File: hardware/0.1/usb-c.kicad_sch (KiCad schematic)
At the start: 30 parts, among them J201 USB_C_Receptacle, U201 TPD4EUSB30, U202 HD3SS3220, U203 TPD4EUSB30, U204 TPD4EUSB30

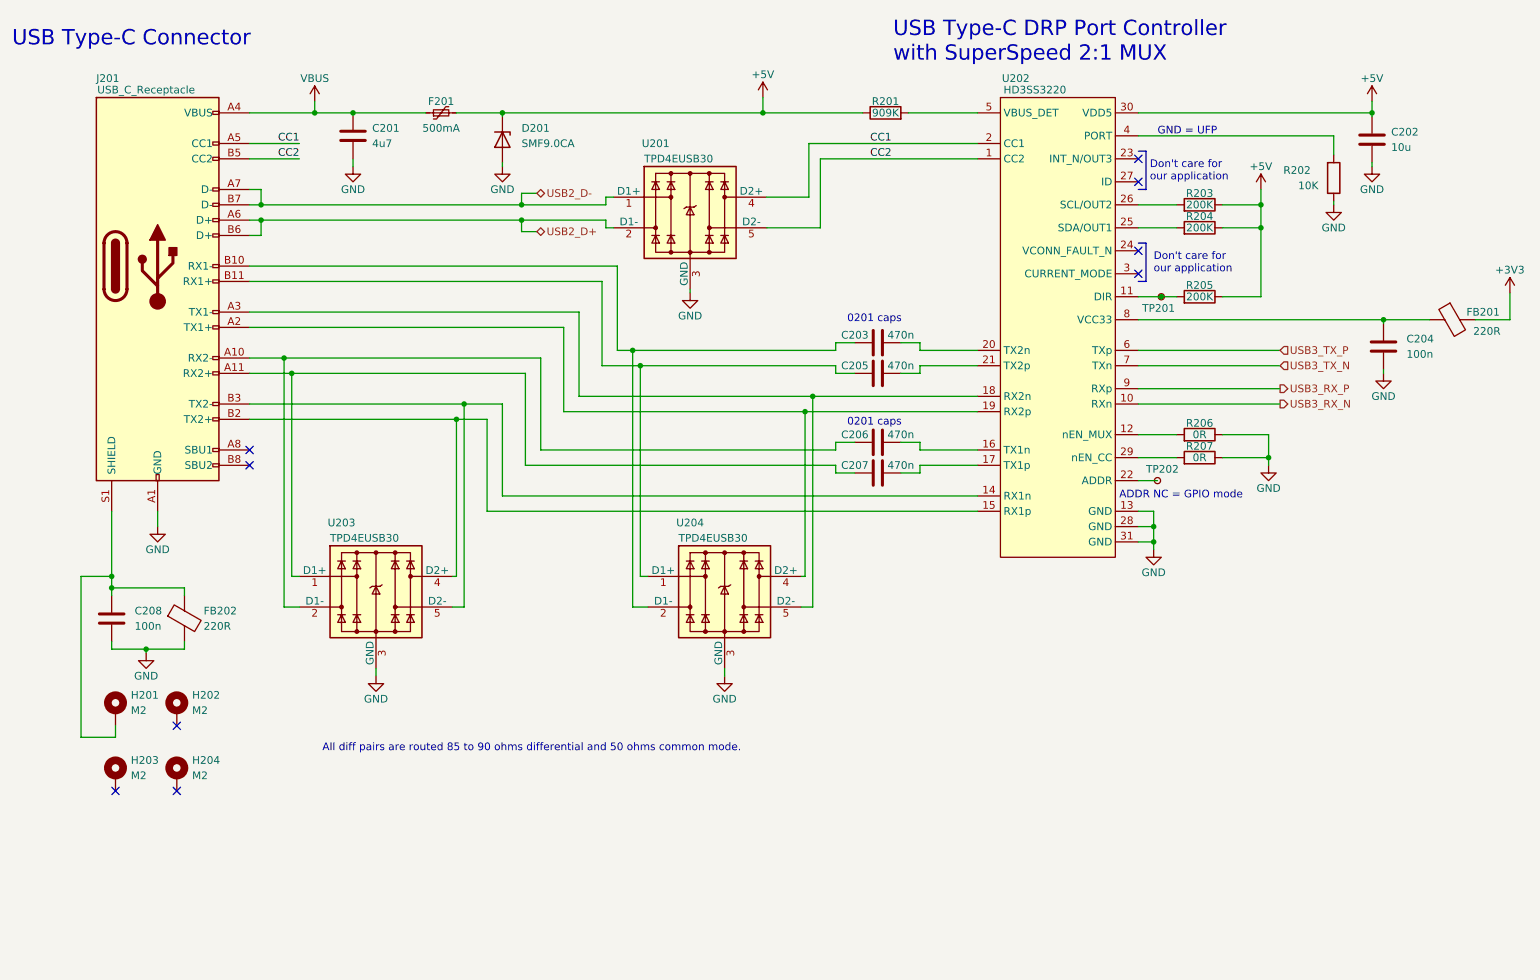
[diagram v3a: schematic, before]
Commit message: break out bga
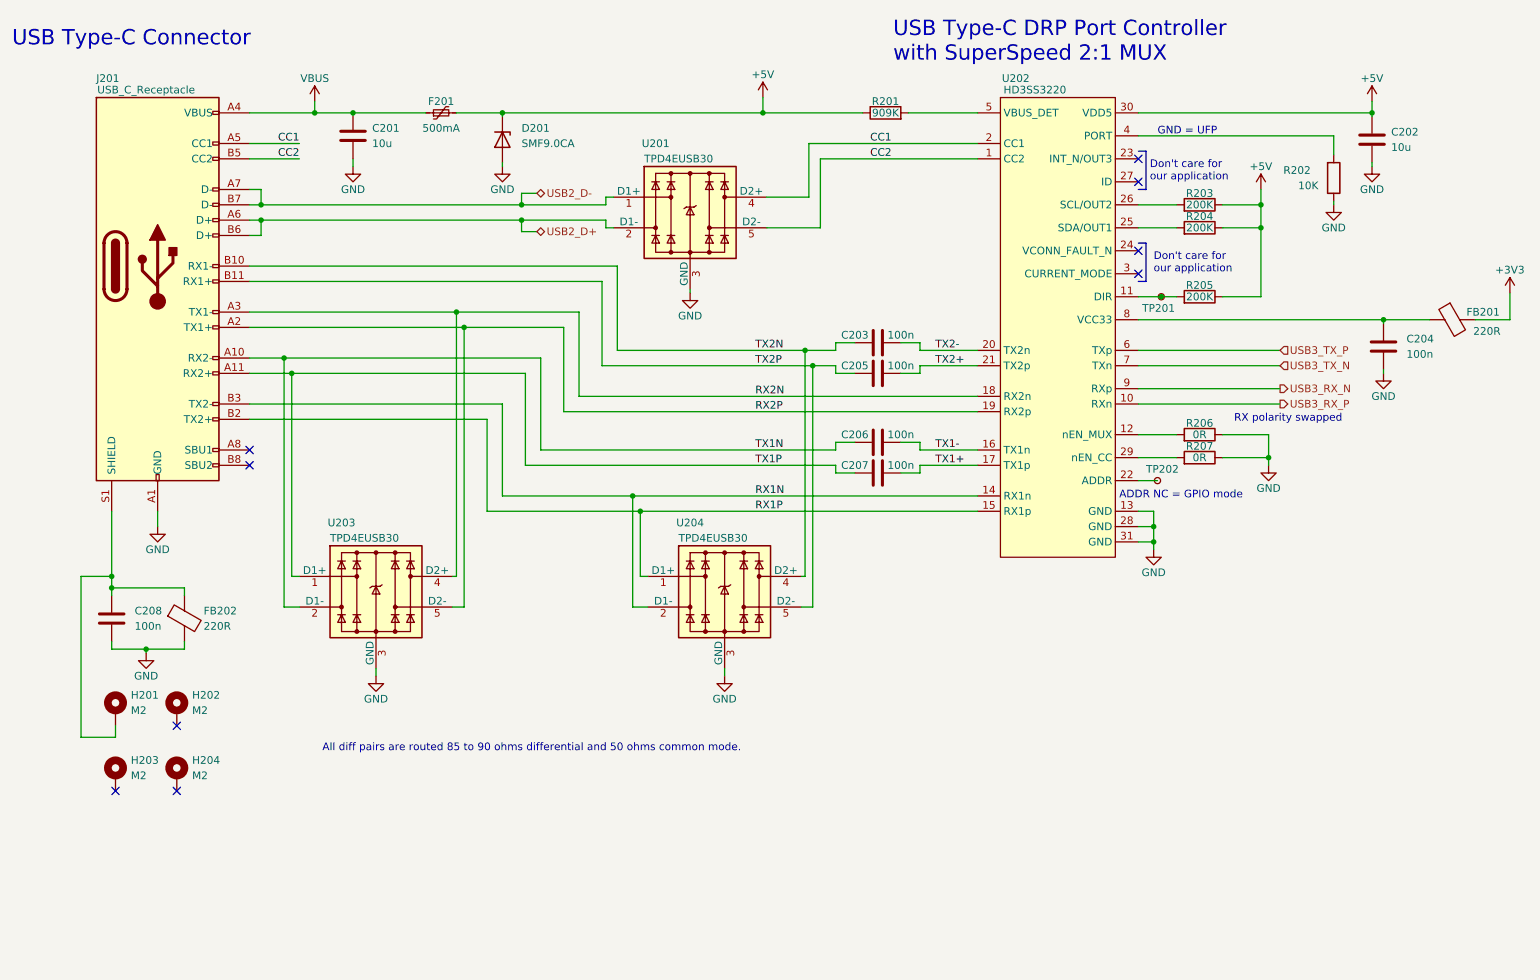
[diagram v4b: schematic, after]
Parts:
- C201: value 4u7 -> 10u; footprint Capacitor_SMD:C_0402_1005Metric -> Capacitor_SMD:C_0603_1608Metric; LCSC C23733 -> (none); MPN CL05A475MP5NRNC -> (none); Manufacturer Samsung Electro-Mechanics -> (none)
- C203, C205, C206, C207: value 470n -> 100n; footprint Capacitor_SMD:C_0402_1005Metric -> Capacitor_SMD:C_0201_0603Metric
- F201: footprint josh-passives-smt:Fuse_0603_1608Metric -> josh-passives-smt:Fuse_0805_2012Metric; LCSC C210357 -> (none); MPN MF-FSMF050X-2 -> (none); Manufacturer Bourns -> (none)
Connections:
- net USB3_RX_N: now also U202.9 (RXp); no longer U202.10 (RXn)
- net USB3_RX_P: now also U202.10 (RXn); no longer U202.9 (RXp)
- net TX1P: now reaches C207.1, J201.A11 (RX2+), U203.1 (D1+)
- net TX1N: now reaches C206.1, J201.A10 (RX2-), U203.2 (D1-)
- net RX1P: now reaches J201.B2 (TX2+), U202.15 (RX1p)
- net RX1P: now also U204.1 (D1+); no longer U203.4 (D2+)
- net RX1N: now reaches J201.B3 (TX2-), U202.14 (RX1n)
- net RX1N: now also U204.2 (D1-); no longer U203.5 (D2-)
- net TX2P: now reaches C205.1, J201.B11 (RX1+)
- net TX2P: now also U204.5 (D2-); no longer U204.1 (D1+)
- net TX2+: now reaches C205.2, U202.21 (TX2p)
- net TX2N: now reaches C203.1, J201.B10 (RX1-)
- net TX2N: now also U204.4 (D2+); no longer U204.2 (D1-)
- net RX2P: now reaches J201.A2 (TX1+), U202.19 (RX2p)
- net RX2P: now also U203.5 (D2-); no longer U204.4 (D2+)
- net RX2N: now reaches J201.A3 (TX1-), U202.18 (RX2n)
- net RX2N: now also U203.4 (D2+); no longer U204.5 (D2-)
- net TX1+: now reaches C207.2, U202.17 (TX1p)
- net TX1-: now reaches C206.2, U202.16 (TX1n)
- net TX2-: now reaches C203.2, U202.20 (TX2n)
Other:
- note added: "RX polarity swapped"
- note removed: "0201 caps"

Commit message: usb3 routed less tuning
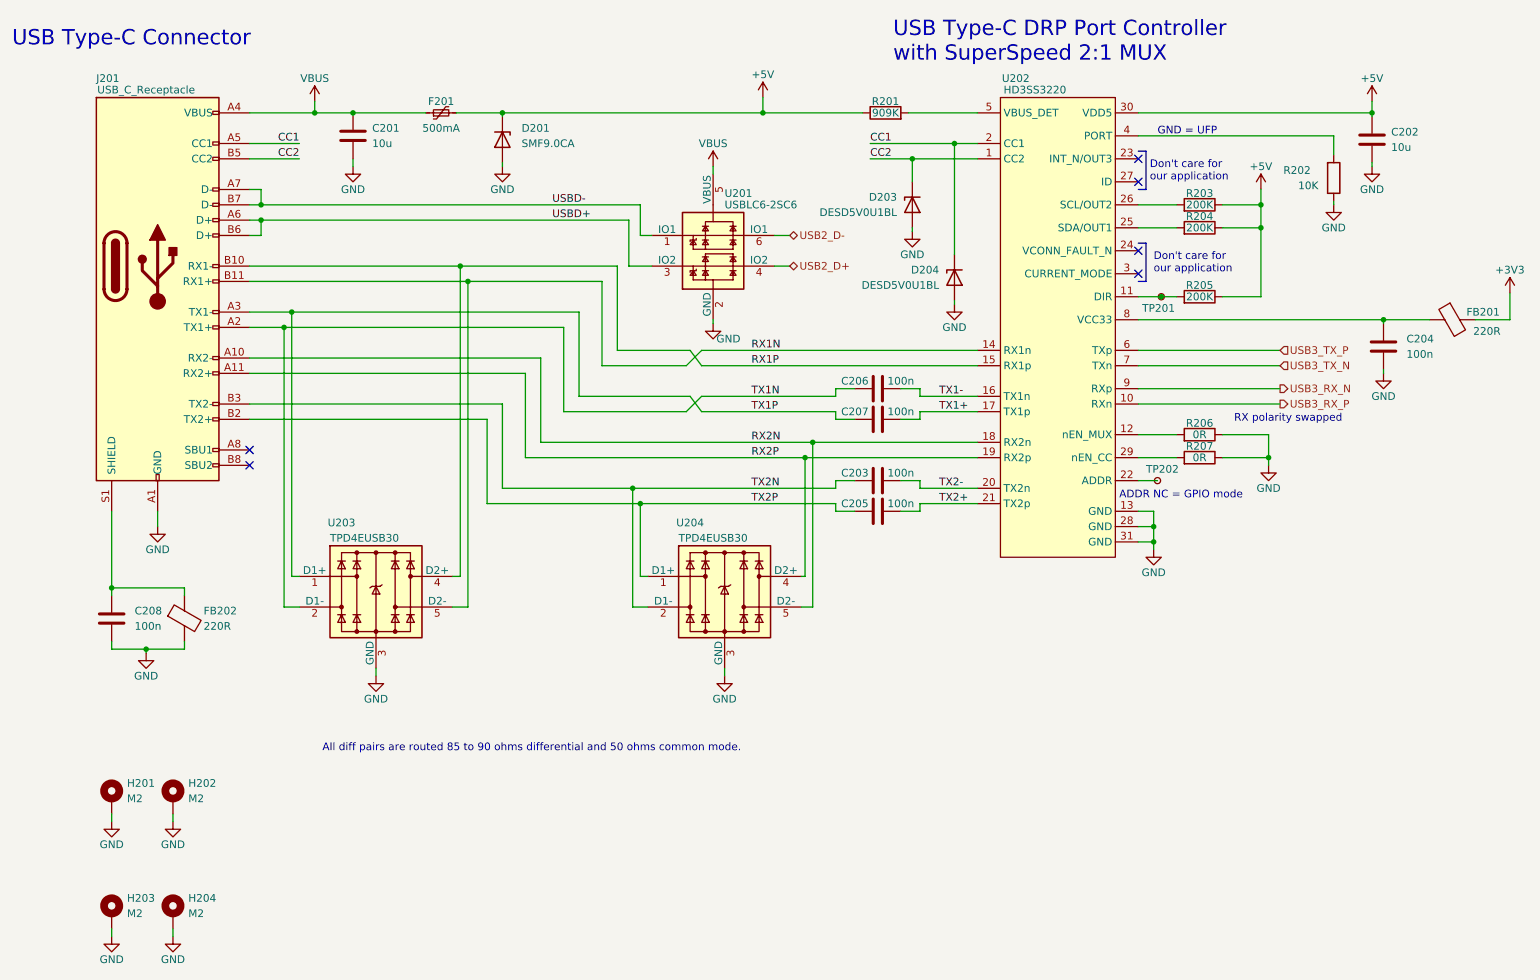
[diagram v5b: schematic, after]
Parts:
- removed U201: TPD4EUSB30, Package_SON:USON-10_2.5x1.0mm_P0.5mm, symbol Power_Protection:TPD4EUSB30
- added D203, D204: DESD5V0U1BL, josh-passives-smt:D_X1-DFN1006-2, symbol Device:D_Zener
- added U201: USBLC6-2SC6, josh-soic-sot-etc:SOT-563, symbol josh-ic:USBLC6-2SC6
- U203, U204: symbol Power_Protection:TPD4EUSB30 -> josh-ic:TPD4EUSB30
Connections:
- net CC1: now also D204.1 (K)
- net CC2: now also D203.1 (K)
- net GND: now also H201.1, H202.1, H203.1, H204.1, D203.2 (A), D204.2 (A), U201.2 (GND)
- net RX1N: now also J201.B11 (RX1+), U203.5 (D2-), U203.6 (NC); no longer J201.B3 (TX2-), U204.2 (D1-)
- net RX1P: now also J201.B10 (RX1-), U203.4 (D2+), U203.7 (NC); no longer J201.B2 (TX2+), U204.1 (D1+)
- net RX2N: now also J201.A10 (RX2-), U204.5 (D2-), U204.6 (NC); no longer J201.A3 (TX1-), U203.4 (D2+)
- net RX2P: now also J201.A11 (RX2+), U204.4 (D2+), U204.7 (NC); no longer J201.A2 (TX1+), U203.5 (D2-)
- net TX1N: now also J201.A2 (TX1+), U203.9 (NC); no longer J201.A10 (RX2-)
- net TX1P: now also J201.A3 (TX1-), U203.10 (NC); no longer J201.A11 (RX2+)
- net TX2N: now also J201.B3 (TX2-), U204.2 (D1-), U204.9 (NC); no longer J201.B10 (RX1-), U204.4 (D2+)
- net TX2P: now also J201.B2 (TX2+), U204.1 (D1+), U204.10 (NC); no longer J201.B11 (RX1+), U204.5 (D2-)
- net USB2_D+: now also U201.4 (IO2); no longer J201.A6 (D+), J201.B6 (D+)
- net USB2_D-: now also U201.6 (IO1); no longer J201.A7 (D-), J201.B7 (D-)
- net VBUS: now also U201.5 (VBUS)
- net at C208.1, FB202.1, J201.S1 (SHIELD): no longer H201.1
- new net USBD+: J201.A6 (D+), J201.B6 (D+), U201.3 (IO2)
- new net USBD-: J201.A7 (D-), J201.B7 (D-), U201.1 (IO1)
- no-connect marks 9 -> 6
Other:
- moved on the sheet: C203, C205, C206, C207, H201, H202, H203, H204

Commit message: wip, switchers todo
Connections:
- net SHIELD: now reaches C208.1, FB202.1, J201.S1 (SHIELD)
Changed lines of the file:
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@@
+    (effects (font (size 1.27 1.27)) (justify left bottom))
+  )
+  (label "SHIELD" (at 41.91 133.985 0)
     (effects (font (size 1.27 1.27)) (justify left bottom))
   )

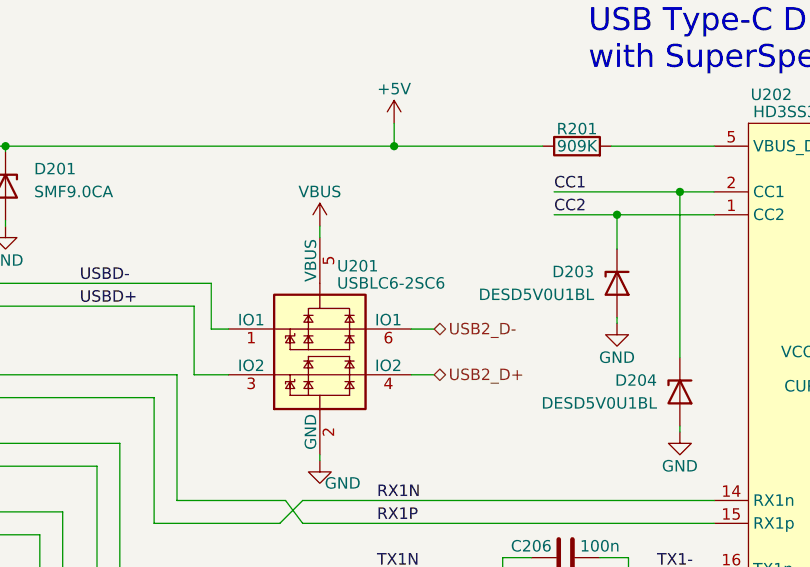
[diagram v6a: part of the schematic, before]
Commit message: erc = drc = 0, fixup BOM
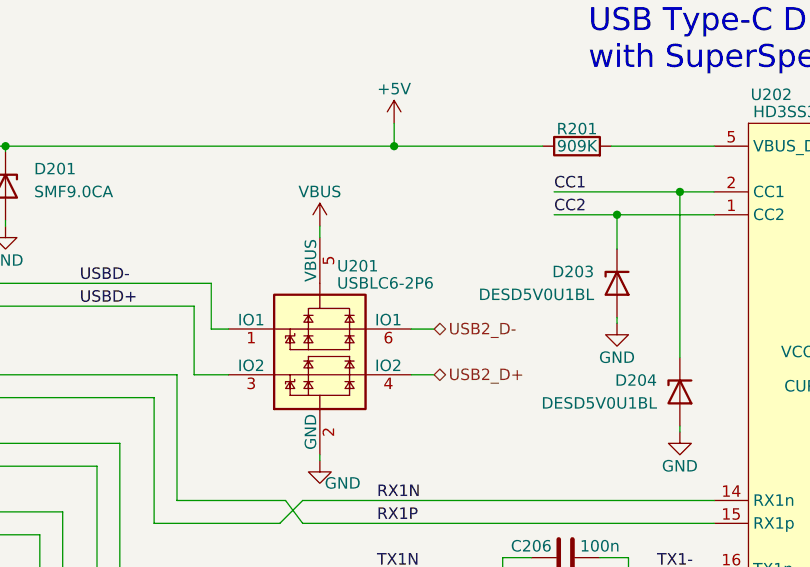
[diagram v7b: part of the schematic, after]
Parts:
- C201: LCSC (none) -> C96446; MPN (none) -> CL10A106MA8NRNC; Manufacturer (none) -> Samsung Electro-Mechanics
- C203, C205, C206, C207: LCSC (none) -> C307380; MPN (none) -> CL03A104KO3NNNC; Manufacturer (none) -> Samsung Electro-Mechanics
- F201: LCSC (none) -> C66452; MPN (none) -> SMD0805-050; Manufacturer (none) -> TECHFUSE
- H201, H202, H203, H204: now left out of the parts list
- R206, R207: MPN RC0402FR-070RL -> C106231; Manufacturer Yageo -> C106231
- U201: value USBLC6-2SC6 -> USBLC6-2P6; LCSC (none) -> C15999; MPN (none) -> USBLC6-2P6; Manufacturer (none) -> STMicroelectronics
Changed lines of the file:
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@@
       (effects (font (size 1.27 1.27)) hide)
     )
-    (property "LCSC" "" (id 4) (at 78.105 59.055 0)
-      (effects (font (size 1.27 1.27)) hide)
-    )
-    (property "MPN" "" (id 5) (at 78.105 59.055 0)
-      (effects (font (size 1.27 1.27)) hide)
-    )
-    (property "Manufacturer" "" (id 6) (at 78.105 59.055 0)
+    (property "LCSC" "C96446" (id 4) (at 78.105 59.055 0)
+      (effects (font (size 1.27 1.27)) hide)
+    )
+    (property "MPN" "CL10A106MA8NRNC" (id 5) (at 78.105 59.055 0)
+      (effects (font (size 1.27 1.27)) hide)
+    )
+    (property "Manufacturer" "Samsung Electro-Mechanics" (id 6) (at 78.105 59.055 0)
       (effects (font (size 1.27 1.27)) hide)
     )
@@
   )
   (symbol (lib_id "Mechanical:MountingHole_Pad") (at 38.1 168.91 0) (unit 1)
-    (in_bom yes) (on_board yes) (fields_autoplaced)
+    (in_bom no) (on_board yes) (fields_autoplaced)
     (property "Reference" "H201" (id 0) (at 40.64 166.3699 0)
       (effects (font (size 1.27 1.27)) (justify left))
@@
     )
     (property "Datasheet" "~" (id 3) (at 165.1 121.285 0)
+      (effects (font (size 1.27 1.27)) hide)
+    )
+    (property "LCSC" "C307380" (id 4) (at 165.1 121.285 0)
+      (effects (font (size 1.27 1.27)) hide)
+    )
+    (property "MPN" "CL03A104KO3NNNC" (id 5) (at 165.1 121.285 0)
+      (effects (font (size 1.27 1.27)) hide)
+    )
+    (property "Manufacturer" "Samsung Electro-Mechanics" (id 6) (at 165.1 121.285 0)
       (effects (font (size 1.27 1.27)) hide)
     )
@@
   )
   (symbol (lib_id "Mechanical:MountingHole_Pad") (at 48.26 168.91 0) (unit 1)
-    (in_bom yes) (on_board yes) (fields_autoplaced)
+    (in_bom no) (on_board yes) (fields_autoplaced)
     (property "Reference" "H202" (id 0) (at 50.8 166.3699 0)
       (effects (font (size 1.27 1.27)) (justify left))
@@
       (effects (font (size 1.27 1.27)) hide)
     )
-    (property "MPN" "RC0402FR-070RL" (id 5) (at 218.44 108.585 0)
-      (effects (font (size 1.27 1.27)) hide)
-    )
-    (property "Manufacturer" "Yageo" (id 6) (at 218.44 108.585 0)
+    (property "MPN" "C106231" (id 5) (at 218.44 108.585 0)
+      (effects (font (size 1.27 1.27)) hide)
+    )
+    (property "Manufacturer" "C106231" (id 6) (at 218.44 108.585 0)
       (effects (font (size 1.27 1.27)) hide)
     )
@@
     )
     (property "Datasheet" "~" (id 3) (at 165.1 106.045 0)
+      (effects (font (size 1.27 1.27)) hide)
+    )
+    (property "LCSC" "C307380" (id 4) (at 165.1 106.045 0)
+      (effects (font (size 1.27 1.27)) hide)
+    )
+    (property "MPN" "CL03A104KO3NNNC" (id 5) (at 165.1 106.045 0)
+      (effects (font (size 1.27 1.27)) hide)
+    )
+    (property "Manufacturer" "Samsung Electro-Mechanics" (id 6) (at 165.1 106.045 0)
       (effects (font (size 1.27 1.27)) hide)
     )
@@
       (effects (font (size 1.27 1.27)) hide)
     )
-    (property "MPN" "RC0402FR-070RL" (id 5) (at 218.44 112.395 0)
-      (effects (font (size 1.27 1.27)) hide)
-    )
-    (property "Manufacturer" "Yageo" (id 6) (at 218.44 112.395 0)
+    (property "MPN" "C106231" (id 5) (at 218.44 112.395 0)
+      (effects (font (size 1.27 1.27)) hide)
+    )
+    (property "Manufacturer" "C106231" (id 6) (at 218.44 112.395 0)
       (effects (font (size 1.27 1.27)) hide)
     )
@@
   )
   (symbol (lib_id "Mechanical:MountingHole_Pad") (at 48.26 187.96 0) (unit 1)
-    (in_bom yes) (on_board yes) (fields_autoplaced)
+    (in_bom no) (on_board yes) (fields_autoplaced)
     (property "Reference" "H204" (id 0) (at 50.8 185.4199 0)
       (effects (font (size 1.27 1.27)) (justify left))
@@
       (effects (font (size 1.27 1.27)) (justify left))
     )
-    (property "Value" "USBLC6-2SC6" (id 1) (at 139.7 70.485 0)
+    (property "Value" "USBLC6-2P6" (id 1) (at 139.7 70.485 0)
       (effects (font (size 1.27 1.27)) (justify left))
     )
@@
     )
     (property "Datasheet" "http://www2.st.com/resource/en/datasheet/CD00050750.pdf" (id 3) (at 142.875 69.215 0)
+      (effects (font (size 1.27 1.27)) hide)
+    )
+    (property "LCSC" "C15999" (id 4) (at 137.795 78.105 0)
+      (effects (font (size 1.27 1.27)) hide)
+    )
+    (property "MPN" "USBLC6-2P6" (id 5) (at 137.795 78.105 0)
+      (effects (font (size 1.27 1.27)) hide)
+    )
+    (property "Manufacturer" "STMicroelectronics" (id 6) (at 137.795 78.105 0)
       (effects (font (size 1.27 1.27)) hide)
     )
@@
       (effects (font (size 1.27 1.27)) hide)
     )
-    (property "MPN" "" (id 4) (at 92.71 55.245 0)
-      (effects (font (size 1.27 1.27)) hide)
-    )
-    (property "Manufacturer" "" (id 5) (at 92.71 55.245 0)
-      (effects (font (size 1.27 1.27)) hide)
-    )
-    (property "LCSC" "" (id 6) (at 92.71 55.245 0)
+    (property "MPN" "SMD0805-050" (id 4) (at 92.71 55.245 0)
+      (effects (font (size 1.27 1.27)) hide)
+    )
+    (property "Manufacturer" "TECHFUSE" (id 5) (at 92.71 55.245 0)
+      (effects (font (size 1.27 1.27)) hide)
+    )
+    (property "LCSC" "C66452" (id 6) (at 92.71 55.245 0)
       (effects (font (size 1.27 1.27)) hide)
     )
@@
       (effects (font (size 1.27 1.27)) hide)
     )
+    (property "LCSC" "C307380" (id 4) (at 165.1 100.965 0)
+      (effects (font (size 1.27 1.27)) hide)
+    )
+    (property "MPN" "CL03A104KO3NNNC" (id 5) (at 165.1 100.965 0)
+      (effects (font (size 1.27 1.27)) hide)
+    )
+    (property "Manufacturer" "Samsung Electro-Mechanics" (id 6) (at 165.1 100.965 0)
+      (effects (font (size 1.27 1.27)) hide)
+    )
     (pin "1")
     (pin "2")
@@
       (effects (font (size 1.27 1.27)) hide)
     )
+    (property "LCSC" "C307380" (id 4) (at 165.1 116.205 0)
+      (effects (font (size 1.27 1.27)) hide)
+    )
+    (property "MPN" "CL03A104KO3NNNC" (id 5) (at 165.1 116.205 0)
+      (effects (font (size 1.27 1.27)) hide)
+    )
+    (property "Manufacturer" "Samsung Electro-Mechanics" (id 6) (at 165.1 116.205 0)
+      (effects (font (size 1.27 1.27)) hide)
+    )
     (pin "1")
     (pin "2")
@@
   )
   (symbol (lib_id "Mechanical:MountingHole_Pad") (at 38.1 187.96 0) (unit 1)
-    (in_bom yes) (on_board yes) (fields_autoplaced)
+    (in_bom no) (on_board yes) (fields_autoplaced)
     (property "Reference" "H203" (id 0) (at 40.64 185.4199 0)
       (effects (font (size 1.27 1.27)) (justify left))

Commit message: component shortage changes
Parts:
- R206, R207: MPN C106231 -> RC0402FR-070RL
- U203, U204: LCSC 296-28063-1-ND -> C90627
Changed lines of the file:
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@@
       (effects (font (size 1.27 1.27)) hide)
     )
-    (property "LCSC" "296-28063-1-ND" (id 7) (at 81.915 134.62 0)
+    (property "LCSC" "C90627" (id 7) (at 81.915 134.62 0)
       (effects (font (size 1.27 1.27)) hide)
     )
@@
       (effects (font (size 1.27 1.27)) hide)
     )
-    (property "LCSC" "296-28063-1-ND" (id 7) (at 139.7 134.62 0)
+    (property "LCSC" "C90627" (id 7) (at 139.7 134.62 0)
       (effects (font (size 1.27 1.27)) hide)
     )
@@
       (effects (font (size 1.27 1.27)) hide)
     )
-    (property "MPN" "C106231" (id 5) (at 218.44 108.585 0)
+    (property "MPN" "RC0402FR-070RL" (id 5) (at 218.44 108.585 0)
       (effects (font (size 1.27 1.27)) hide)
     )
@@
       (effects (font (size 1.27 1.27)) hide)
     )
-    (property "MPN" "C106231" (id 5) (at 218.44 112.395 0)
-      (effects (font (size 1.27 1.27)) hide)
-    )
+    (property "MPN" "RC0402FR-070RL" (id 5) (at 218.44 112.395 0)
+      (effects (font (size 1.27 1.27)) hide)
+    )
